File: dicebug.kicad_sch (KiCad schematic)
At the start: 56 parts, among them J3 PMOD, Q1 SSM6N35AFE, U1 74LV163ADR, U2 MTCH1010, U3 74HCS7266DR, U4 MIC5205YM5, U5 iqs211a

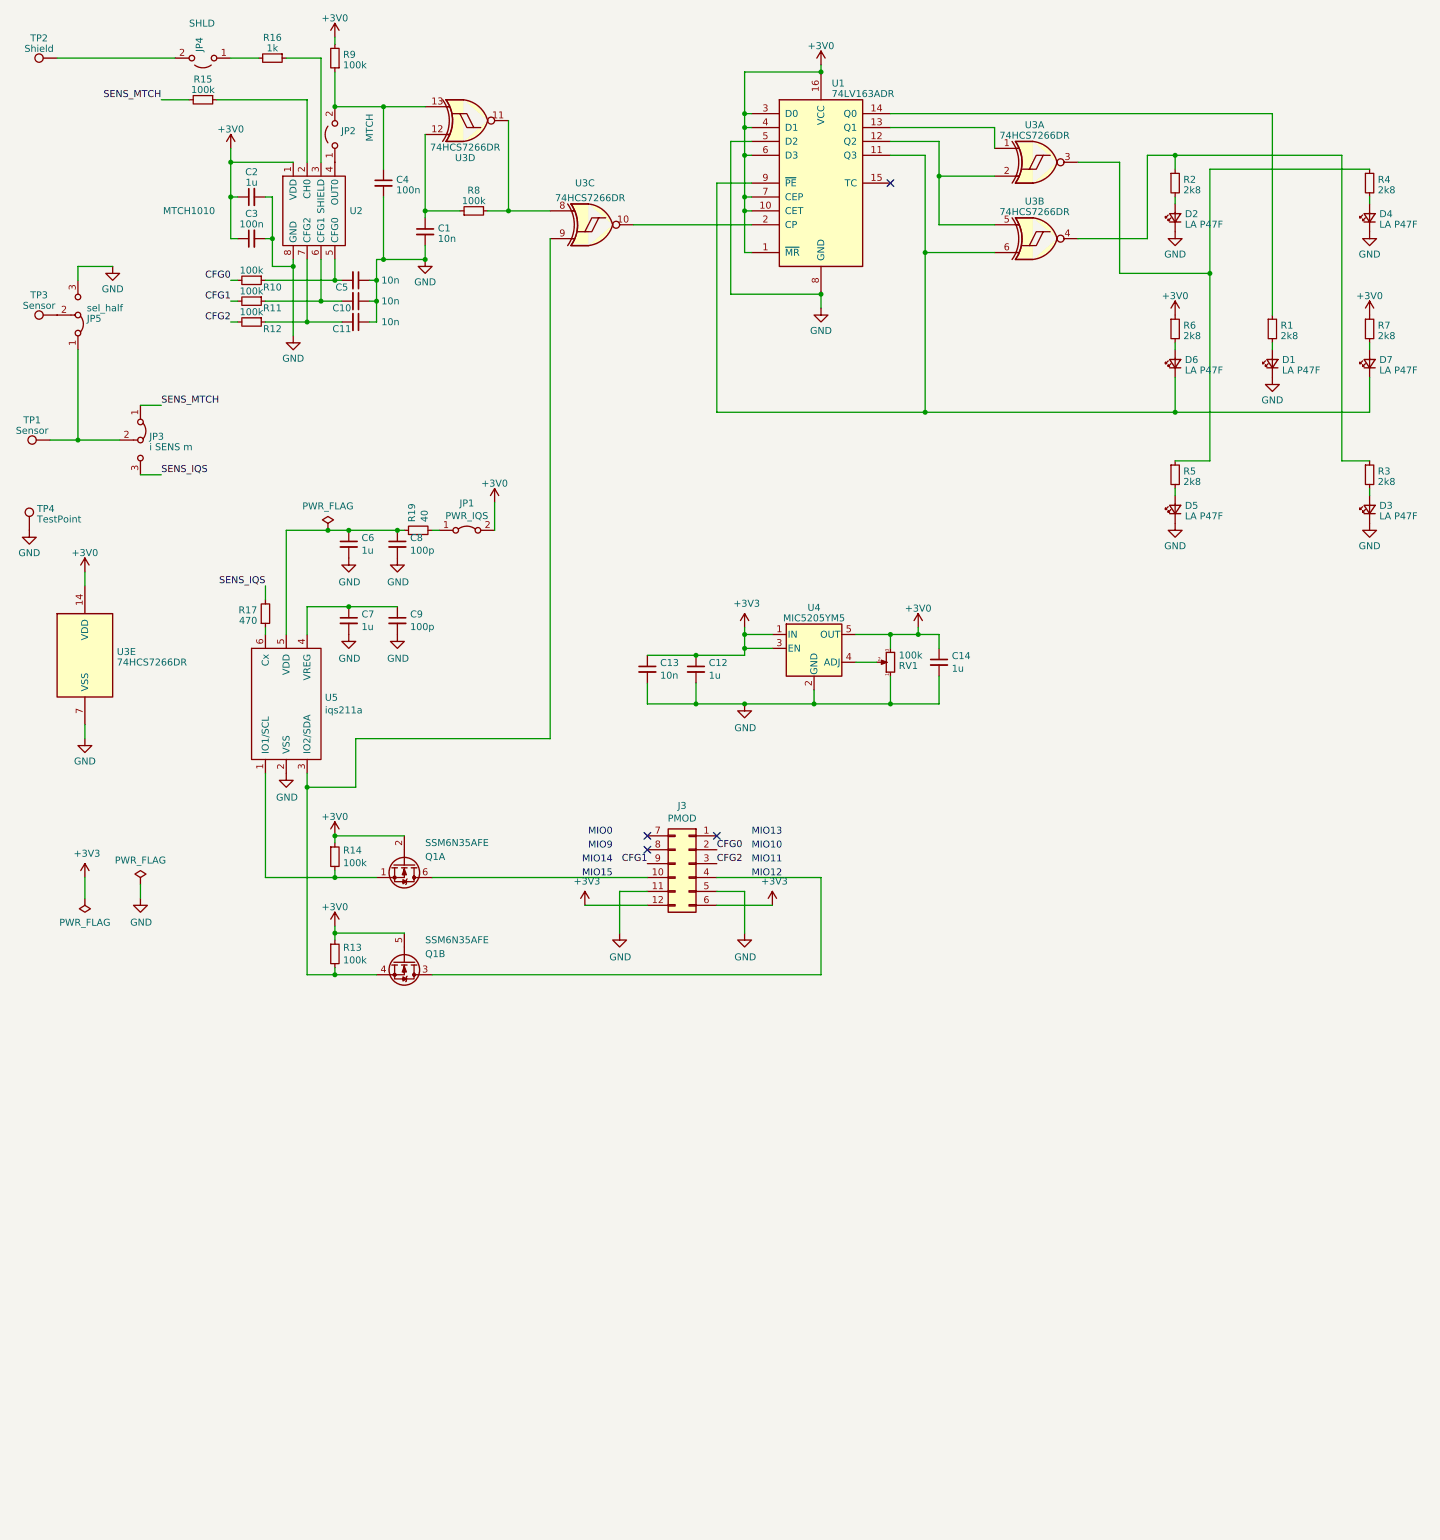
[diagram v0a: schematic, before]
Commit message: almost finalized with individual LED resistors, though
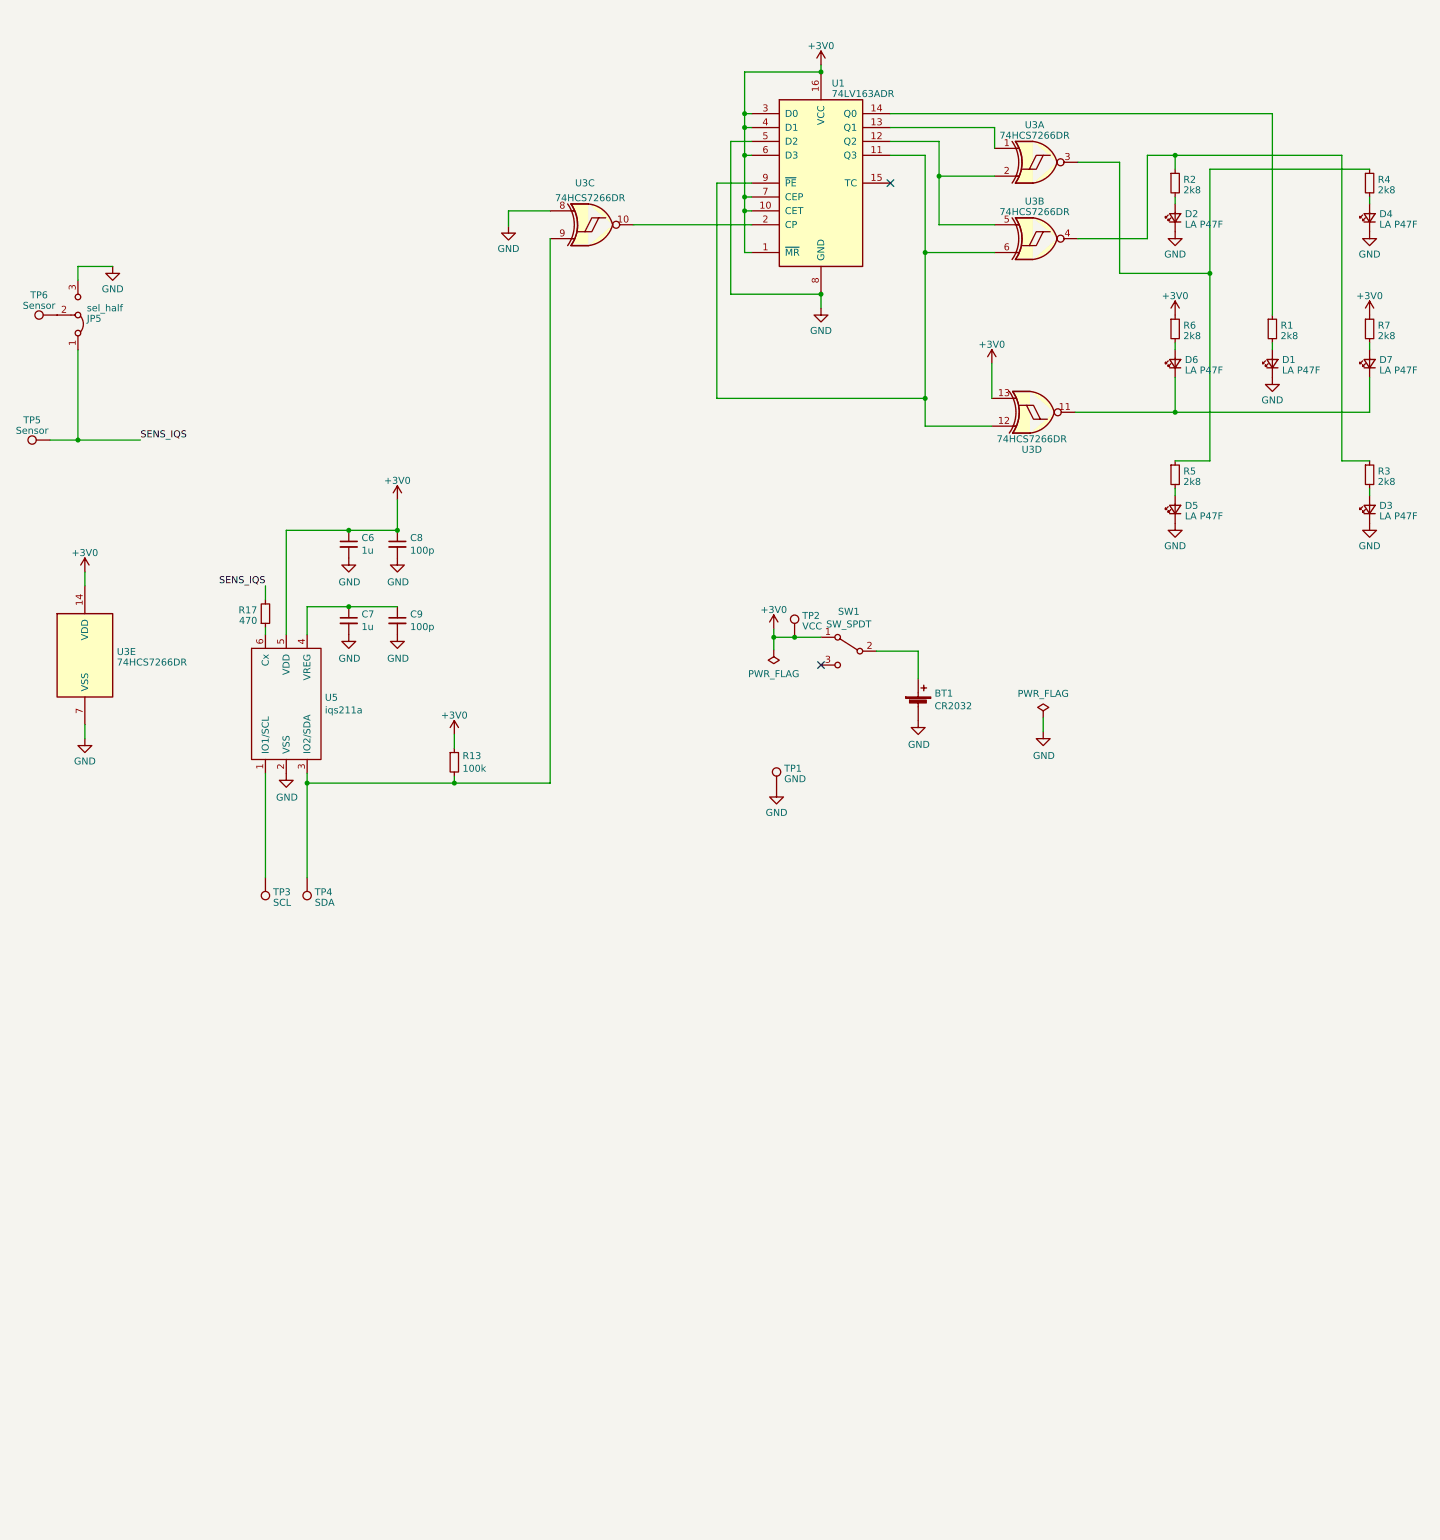
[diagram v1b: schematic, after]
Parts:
- removed C1, C10, C11, C13, C5: 10n, Capacitor_SMD:C_0805_2012Metric, symbol Device:C_Small
- removed C12, C2: 1u, Capacitor_SMD:C_1206_3216Metric, symbol Device:C_Small
- removed C14: 1u, Capacitor_SMD:C_0805_2012Metric, symbol Device:C_Small
- removed C3, C4: 100n, Capacitor_SMD:C_0805_2012Metric, symbol Device:C_Small
- removed J3: PMOD, proj_footprints:PMOD_PinHeader_2x06_P2.54mm_Horizontal, symbol Connector_Generic:Conn_02x06_Top_Bottom
- removed JP1: PWR_IQS, Connector_PinHeader_2.54mm:PinHeader_1x02_P2.54mm_Vertical, symbol Jumper:Jumper_2_Bridged
- removed JP2: MTCH, Connector_PinHeader_1.27mm:PinHeader_1x02_P1.27mm_Vertical, symbol Jumper:Jumper_2_Open
- removed JP3: i SENS m, Connector_PinHeader_1.27mm:PinHeader_1x03_P1.27mm_Vertical, symbol Jumper:Jumper_3_Bridged12
- removed JP4: SHLD, Connector_PinHeader_1.27mm:PinHeader_1x02_P1.27mm_Vertical, symbol Jumper:Jumper_2_Open
- removed Q1: SSM6N35AFE, proj_footprints:SOT-563-adjusted, symbol Device:Q_Dual_NMOS_S1G1D2S2G2D1
- removed R10, R11, R12, R14, R15, R8, R9: 100k, Resistor_SMD:R_0805_2012Metric, symbol Device:R_Small
- removed R16: 1k, Resistor_SMD:R_0805_2012Metric, symbol Device:R_Small
- removed R19: 40, Resistor_SMD:R_0805_2012Metric, symbol Device:R_Small
- removed RV1: 100k, Potentiometer_SMD:Potentiometer_Bourns_TC33X_Vertical, symbol Device:R_Potentiometer_Small
- removed U2: MTCH1010, Package_SO:SOIC-8_3.9x4.9mm_P1.27mm, symbol fmc:MTCH1010
- removed U4: MIC5205YM5, Package_TO_SOT_SMD:SOT-23-5, symbol Regulator_Linear:MIC5205YM5
- added BT1: CR2032, Battery:BatteryHolder_Keystone_3034_1x20mm, symbol Device:Battery_Cell
- added SW1: SW_SPDT, proj_footprints:450404015514, symbol Switch:SW_SPDT
- added TP3: SCL, TestPoint:TestPoint_Pad_D2.0mm, symbol Connector:TestPoint
- added TP4: SDA, TestPoint:TestPoint_Pad_D2.0mm, symbol Connector:TestPoint
- TP1: renamed from TP4; value TestPoint -> GND; footprint Connector_PinHeader_2.54mm:PinHeader_1x01_P2.54mm_Vertical -> TestPoint:TestPoint_Pad_D2.0mm
- TP2: value Shield -> VCC; footprint sensors:tp_end -> TestPoint:TestPoint_Pad_D2.0mm
- renumbered TP1 to TP5, TP3 to TP6
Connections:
- net +3V0: now also C6.1, C8.1, TP2.1, U3.13, U5.5 (VDD), SW1.1 (A)
- net GND: now also U3.8, BT1.2 (-)
- net SENS_IQS: now also JP5.1 (A), TP5.1
- net at U3.11: now also D6.1 (K), D7.1 (K); no longer U3.8
- net at R13.2, U3.9, U5.3 (IO2/SDA): now also TP4.1
- net at U3.12: now also U1.11 (Q3), U1.9 (~{PE}), U3.6
- net at U5.1 (IO1/SCL): now also TP3.1
- new net: BT1.1 (+), SW1.2 (B)
- no-connect marks 4 -> 2
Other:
- note removed: "MIO0"
- note removed: "MIO10"
- note removed: "MIO11"
- note removed: "MIO12"
- note removed: "MIO13"
- note removed: "MIO14"
- note removed: "MIO15"
- note removed: "MIO9"
- moved on the sheet: R13, TP1, U3D

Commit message: Drew schematics for R-array version; works fine.
No layout; the problem is that there is no reasonably priced
resistor array in SIOC-16 :-(
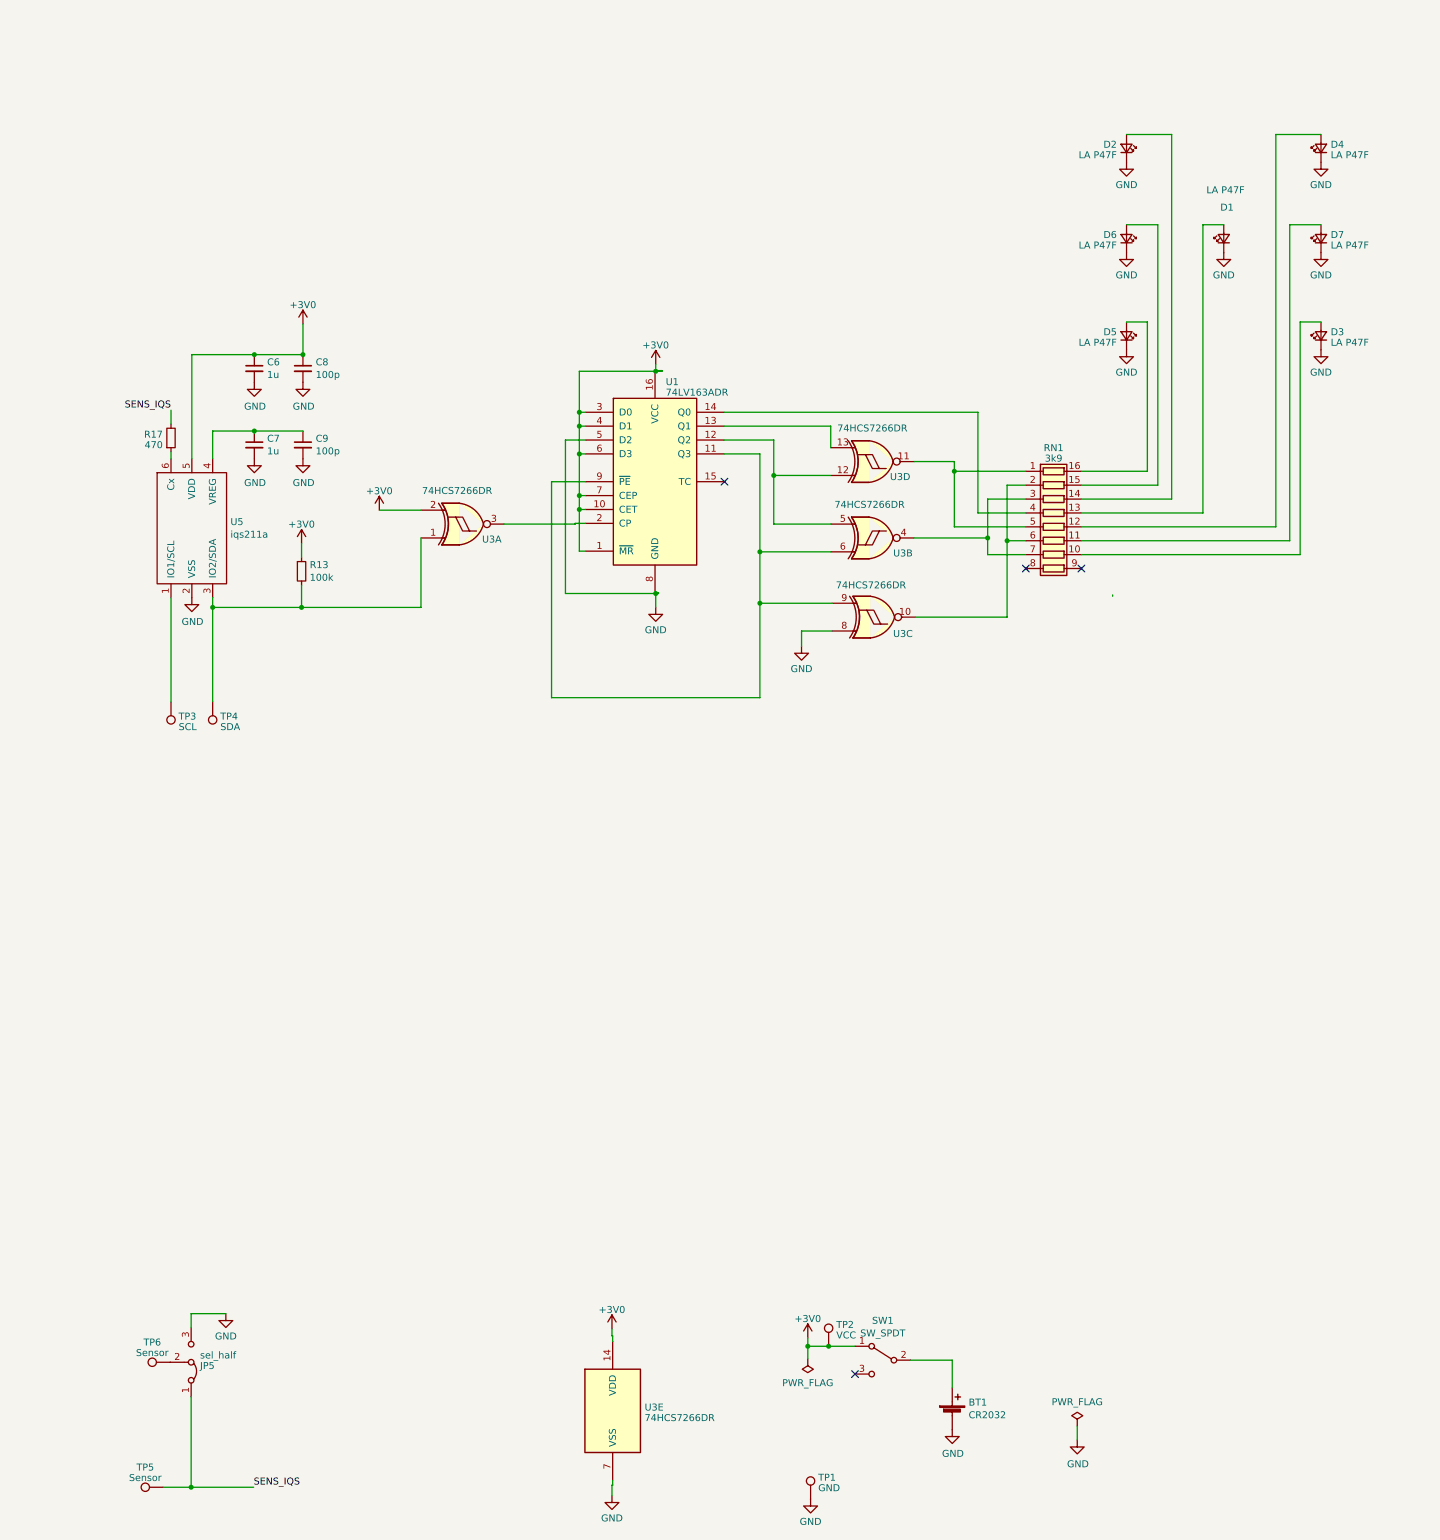
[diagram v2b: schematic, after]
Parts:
- removed R1, R2, R3, R4, R5, R6, R7: 2k8, Resistor_SMD:R_0805_2012Metric, symbol Device:R_Small
- added RN1: 3k9, Resistor_SMD:R_Array_Convex_8x0602, symbol Device:R_Pack08
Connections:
- net +3V0: now also U3.2; no longer U3.13
- net GND: now also D6.1 (K), D7.1 (K)
- net at U3.10: now also RN1.2 (R2.1), RN1.6 (R6.1); no longer U1.2 (CP)
- net at R13.2, TP4.1, U5.3 (IO2/SDA): now also U3.1; no longer U3.9
- net at D6.2 (A): now also RN1.15 (R2.2)
- net at U1.11 (Q3), U1.9 (~{PE}), U3.6: now also U3.9; no longer U3.12
- net at U1.12 (Q2), U3.5: now also U3.12; no longer U3.2
- net at U1.13 (Q1): now also U3.13; no longer U3.1
- net at U1.14 (Q0): now also RN1.4 (R4.1)
- net at U3.4: now also RN1.3 (R3.1), RN1.7 (R7.1)
- net at D3.2 (A): now also RN1.10 (R7.2)
- net at D4.2 (A): now also RN1.12 (R5.2)
- net at D7.2 (A): now also RN1.11 (R6.2)
- net at D2.2 (A): now also RN1.14 (R3.2)
- net at U3.3: now also U1.2 (CP)
- net at D5.2 (A): now also RN1.16 (R1.2)
- net at D1.2 (A): now also RN1.13 (R4.2)
- new net: RN1.1 (R1.1), RN1.5 (R5.1), U3.11
- no-connect marks 2 -> 4
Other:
- moved on the sheet: BT1, C6, C7, C8, C9, D1, D2, D3, D4, D5, D6, D7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
